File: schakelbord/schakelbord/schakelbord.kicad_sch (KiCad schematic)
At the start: 103 parts, among them J1 Rookmachine, J12 I/O nano, J15 Relais 7&8, J16 Alalog i/o, J17 Extra 1-4, J18 Extra 5-8, J19 Relais 5&6, J20 Relais 3&4, J21 Relais 1&2, J3 Power, J4 mosfets, K10 SANYOU_SRD_Form_C, K3 SANYOU_SRD_Form_C, K4 SANYOU_SRD_Form_C, K5 SANYOU_SRD_Form_C, K6 SANYOU_SRD_Form_C, K7 SANYOU_SRD_Form_C, K8 SANYOU_SRD_Form_C, K9 SANYOU_SRD_Form_C, Q1 BC547, Q10 BC337, Q11 BC337, Q12 BC337, Q13 BC337, Q14 BC337, Q4 Q_NMOS_GSD, Q5 BC337, Q6 BC337, Q7 Q_NMOS_GSD, Q8 Q_NMOS_GSD, Q9 BC337, U1 MCP23017x-x-SP

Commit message: pcb update
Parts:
- J1, J3: footprint PCM_SparkFun-Resistor:R_0603_1608Metric -> TerminalBlock_Phoenix:TerminalBlock_Phoenix_MKDS-1,5-2-5.08_1x02_P5.08mm_Horizontal
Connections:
- net at R47.1: now also D36.1 (K)
- net at D35.1 (K): now also R48.1
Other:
- moved on the sheet: D35, D36
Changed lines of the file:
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@@
 	)
 	(junction
-		(at 259.08 250.19)
+		(at 257.81 250.19)
 		(diameter 0)
 		(color 0 0 0 0)
@@
 	)
 	(junction
-		(at 252.73 250.19)
+		(at 251.46 250.19)
 		(diameter 0)
 		(color 0 0 0 0)
@@
 	(wire
 		(pts
-			(xy 259.08 250.19) (xy 264.16 250.19)
-		)
-		(stroke
-			(width 0)
-			(type default)
-		)
-	)
-	(wire
-		(pts
 			(xy 363.22 247.65) (xy 381 247.65)
 		)
@@
 	(wire
 		(pts
-			(xy 246.38 250.19) (xy 252.73 250.19)
+			(xy 246.38 250.19) (xy 264.16 250.19)
 		)
 		(stroke
@@
 	(wire
 		(pts
-			(xy 252.73 250.19) (xy 259.08 250.19)
-		)
-		(stroke
-			(width 0)
-			(type default)
-		)
-	)
-	(wire
-		(pts
 			(xy 87.63 255.27) (xy 91.44 255.27)
 		)
@@
 			)
 		)
-		(property "Footprint" "PCM_SparkFun-Resistor:R_0603_1608Metric"
+		(property "Footprint" "TerminalBlock_Phoenix:TerminalBlock_Phoenix_MKDS-1,5-2-5.08_1x02_P5.08mm_Horizontal"
 			(at 67.31 365.76 0)
 			(hide yes)
@@
 	(symbol
 		(lib_id "Device:LED")
-		(at 259.08 254 90)
+		(at 257.81 254 90)
 		(unit 1)
 		(body_style 1)
@@
 		(fields_autoplaced yes)
 		(property "Reference" "D35"
-			(at 256.54 256.8576 90)
+			(at 255.27 256.8576 90)
 			(show_name no)
 			(do_not_autoplace no)
@@
 		)
 		(property "Value" "LED"
-			(at 256.54 254.3176 90)
+			(at 255.27 254.3176 90)
 			(hide yes)
 			(show_name no)
@@
 		)
 		(property "Footprint" "LED_THT:LED_D5.0mm"
-			(at 259.08 254 0)
+			(at 257.81 254 0)
 			(hide yes)
 			(show_name no)
@@
 		)
 		(property "Datasheet" ""
-			(at 259.08 254 0)
+			(at 257.81 254 0)
 			(hide yes)
 			(show_name no)
@@
 		)
 		(property "Description" "Light emitting diode"
-			(at 259.08 254 0)
+			(at 257.81 254 0)
 			(hide yes)
 			(show_name no)
@@
 		)
 		(property "Sim.Pins" "1=K 2=A"
-			(at 259.08 254 0)
+			(at 257.81 254 0)
 			(hide yes)
 			(show_name no)
@@
 	(symbol
 		(lib_id "Device:LED")
-		(at 252.73 254 90)
+		(at 251.46 254 90)
 		(unit 1)
 		(body_style 1)
@@
 		(fields_autoplaced yes)
 		(property "Reference" "D36"
-			(at 250.19 256.8576 90)
+			(at 248.92 256.8576 90)
 			(show_name no)
 			(do_not_autoplace no)
@@
 		)
 		(property "Value" "LED"
-			(at 250.19 254.3176 90)
+			(at 248.92 254.3176 90)
 			(hide yes)
 			(show_name no)
@@
 		)
 		(property "Footprint" "LED_THT:LED_D5.0mm"
-			(at 252.73 254 0)
+			(at 251.46 254 0)
 			(hide yes)
 			(show_name no)
@@
 		)
 		(property "Datasheet" ""
-			(at 252.73 254 0)
+			(at 251.46 254 0)
 			(hide yes)
 			(show_name no)
@@
 		)
 		(property "Description" "Light emitting diode"
-			(at 252.73 254 0)
+			(at 251.46 254 0)
 			(hide yes)
 			(show_name no)
@@
 		)
 		(property "Sim.Pins" "1=K 2=A"
-			(at 252.73 254 0)
+			(at 251.46 254 0)
 			(hide yes)
 			(show_name no)
@@
 			)
 		)
-		(property "Footprint" "PCM_SparkFun-Resistor:R_0603_1608Metric"
+		(property "Footprint" "TerminalBlock_Phoenix:TerminalBlock_Phoenix_MKDS-1,5-2-5.08_1x02_P5.08mm_Horizontal"
 			(at 195.58 345.44 0)
 			(hide yes)

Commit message: pcb update
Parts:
- removed D15, D16: LED, LED_THT:LED_D5.0mm, symbol Device:LED
- removed Q4, Q7, Q8: Q_NMOS_GSD, PCM_SparkFun-Semiconductor-Standard:SC-89 SOT-490, symbol Transistor_FET:Q_NMOS_GSD
- removed R25, R28: 1K, Resistor_THT:R_Axial_DIN0204_L3.6mm_D1.6mm_P7.62mm_Horizontal, symbol Device:R
- added Q15, Q2, Q3: IRLZ44N, Package_TO_SOT_THT:TO-220-3_Vertical, symbol Transistor_FET:IRLZ44N
- added R61, R62: 470, Resistor_THT:R_Axial_DIN0204_L3.6mm_D1.6mm_P7.62mm_Horizontal, symbol Device:R
- Q1: value BC547 -> BC337
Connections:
- net +3.3V: now also R61.1, R62.1
- net GND: now also D17.1 (K), U1.15 (A0), U1.16 (A1), U1.17 (A2), Q15.3 (S), Q2.3 (S), Q3.3 (S)
- net at R23.2, R24.1: now also Q15.1 (G)
- net at R29.2, R30.1: now also Q2.1 (G)
- net at J4.1 (Pin_1): now also Q2.2 (D); no longer D17.1 (K)
- net at A1.23 (SDA/A4), U1.13 (SDA): now also R62.2
- net at A1.24 (SCL/A5), U1.12 (SCK): now also R61.2
- net at J4.2 (Pin_2): now also Q3.2 (D)
- net at R26.2, R27.1: now also Q3.1 (G)
- net at J4.3 (Pin_3): now also Q15.2 (D)
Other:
- moved on the sheet: J3

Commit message: pcb update
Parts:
- R61, R62: value 470 -> 4k7
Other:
- moved on the sheet: R8
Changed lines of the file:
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@@
 	)
 	(junction
+		(at 203.2 264.16)
+		(diameter 0)
+		(color 0 0 0 0)
+	)
+	(junction
 		(at 274.32 295.91)
 		(diameter 0)
@@
 	(wire
 		(pts
-			(xy 199.39 264.16) (xy 220.98 264.16)
+			(xy 199.39 264.16) (xy 203.2 264.16)
 		)
 		(stroke
@@
 	(wire
 		(pts
-			(xy 199.39 264.16) (xy 199.39 285.75)
-		)
-		(stroke
-			(width 0)
-			(type default)
-		)
-	)
-	(wire
-		(pts
 			(xy 389.89 287.02) (xy 398.78 287.02)
 		)
@@
 	(wire
 		(pts
+			(xy 203.2 274.32) (xy 203.2 300.99)
+		)
+		(stroke
+			(width 0)
+			(type default)
+		)
+	)
+	(wire
+		(pts
 			(xy 430.53 224.79) (xy 430.53 246.38)
 		)
@@
 	(wire
 		(pts
-			(xy 199.39 300.99) (xy 208.28 300.99)
-		)
-		(stroke
-			(width 0)
-			(type default)
-		)
-	)
-	(wire
-		(pts
 			(xy 233.68 303.53) (xy 316.23 303.53)
 		)
@@
 	(wire
 		(pts
+			(xy 203.2 264.16) (xy 203.2 266.7)
+		)
+		(stroke
+			(width 0)
+			(type default)
+		)
+	)
+	(wire
+		(pts
 			(xy 100.33 369.57) (xy 100.33 375.92)
 		)
@@
 	(wire
 		(pts
+			(xy 203.2 264.16) (xy 220.98 264.16)
+		)
+		(stroke
+			(width 0)
+			(type default)
+		)
+	)
+	(wire
+		(pts
 			(xy 233.68 285.75) (xy 251.46 285.75)
 		)
@@
 	(wire
 		(pts
+			(xy 203.2 300.99) (xy 208.28 300.99)
+		)
+		(stroke
+			(width 0)
+			(type default)
+		)
+	)
+	(wire
+		(pts
 			(xy 316.23 303.53) (xy 316.23 152.4)
 		)
@@
 	(wire
 		(pts
-			(xy 199.39 293.37) (xy 199.39 300.99)
-		)
-		(stroke
-			(width 0)
-			(type default)
-		)
-	)
-	(wire
-		(pts
 			(xy 335.28 316.23) (xy 335.28 308.61)
 		)
@@
 		(in_pos_files yes)
 		(dnp no)
-		(fields_autoplaced yes)
 		(property "Reference" "R61"
-			(at 181.61 271.7801 0)
-			(hide yes)
+			(at 189.484 268.224 0)
 			(show_name no)
 			(do_not_autoplace no)
@@
 			)
 		)
-		(property "Value" "470"
+		(property "Value" "4k7"
 			(at 186.69 270.5099 0)
 			(show_name no)
@@
 	(symbol
 		(lib_id "Device:R")
-		(at 199.39 289.56 0)
+		(at 203.2 270.51 0)
 		(unit 1)
 		(body_style 1)
@@
 		(fields_autoplaced yes)
 		(property "Reference" "R8"
-			(at 201.93 288.2899 0)
+			(at 205.74 269.2399 0)
 			(show_name no)
 			(do_not_autoplace no)
@@
 		)
 		(property "Value" "10k"
-			(at 201.93 290.8299 0)
+			(at 205.74 271.7799 0)
 			(show_name no)
 			(do_not_autoplace no)
@@
 		)
 		(property "Footprint" "Resistor_THT:R_Axial_DIN0204_L3.6mm_D1.6mm_P7.62mm_Horizontal"
-			(at 197.612 289.56 90)
+			(at 201.422 270.51 90)
 			(hide yes)
 			(show_name no)
@@
 		)
 		(property "Datasheet" ""
-			(at 199.39 289.56 0)
+			(at 203.2 270.51 0)
 			(hide yes)
 			(show_name no)
@@
 		)
 		(property "Description" "Resistor"
-			(at 199.39 289.56 0)
+			(at 203.2 270.51 0)
 			(hide yes)
 			(show_name no)
@@
 		(in_pos_files yes)
 		(dnp no)
-		(fields_autoplaced yes)
 		(property "Reference" "R62"
-			(at 191.77 271.7801 0)
-			(hide yes)
+			(at 199.39 268.478 0)
 			(show_name no)
 			(do_not_autoplace no)
@@
 			)
 		)
-		(property "Value" "470"
+		(property "Value" "4k7"
 			(at 196.85 270.5099 0)
 			(show_name no)

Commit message: pcb update
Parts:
- removed D10, D11, D12: LED, LED_THT:LED_D5.0mm, symbol Device:LED
- removed R14, R15, R16: 1K, Resistor_THT:R_Axial_DIN0204_L3.6mm_D1.6mm_P7.62mm_Horizontal, symbol Device:R

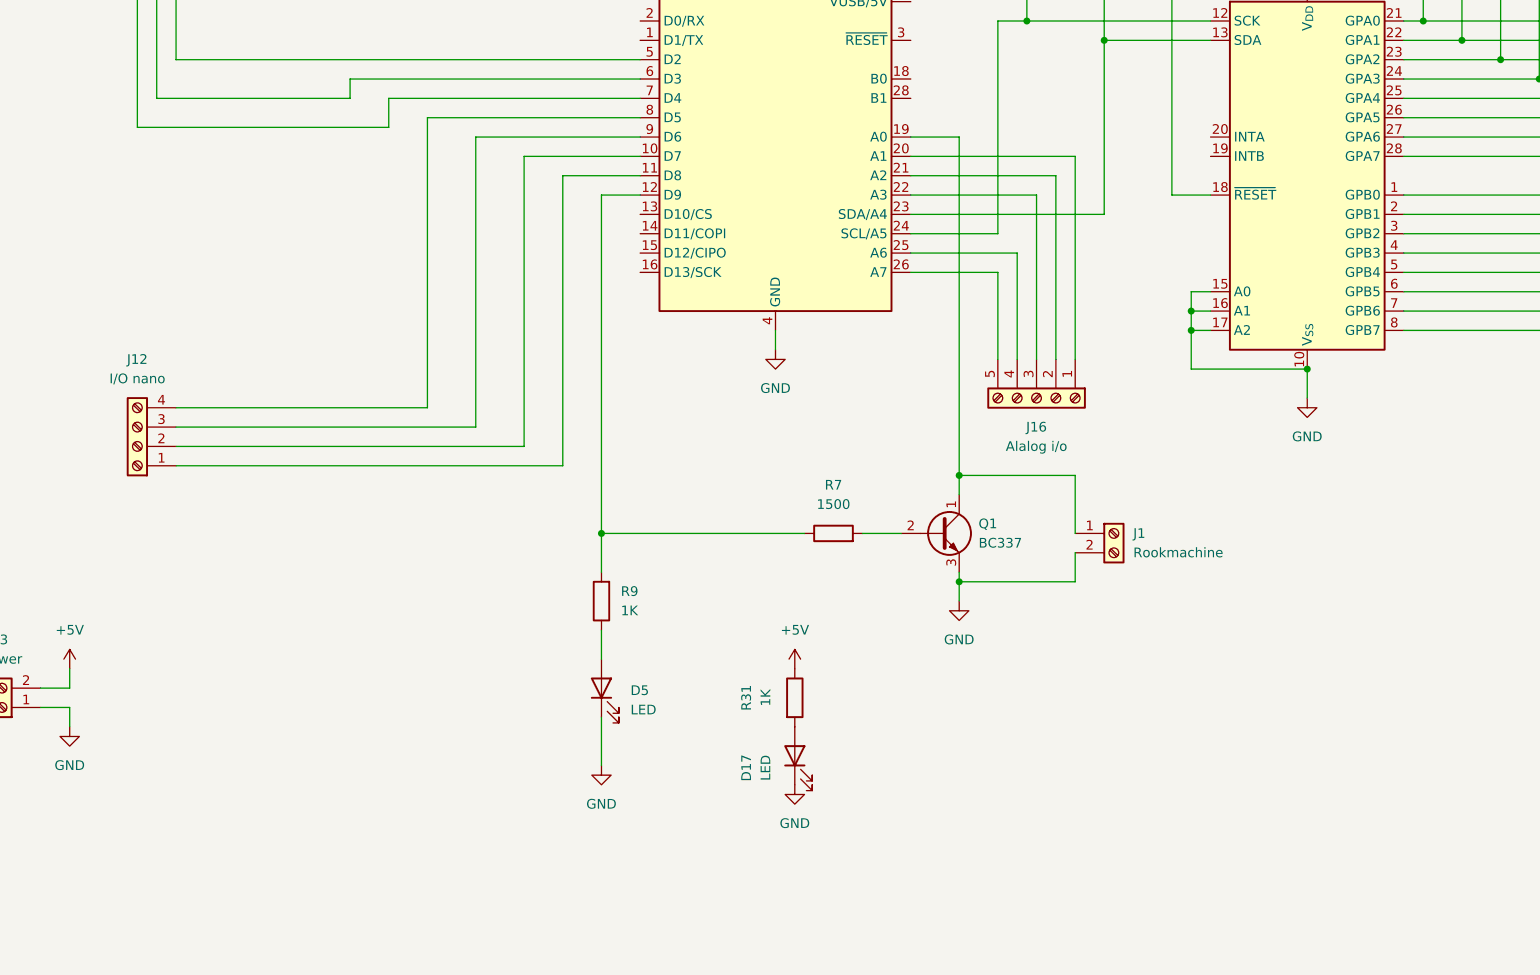
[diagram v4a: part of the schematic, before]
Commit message: Add option to detect if smoke machine is turned on
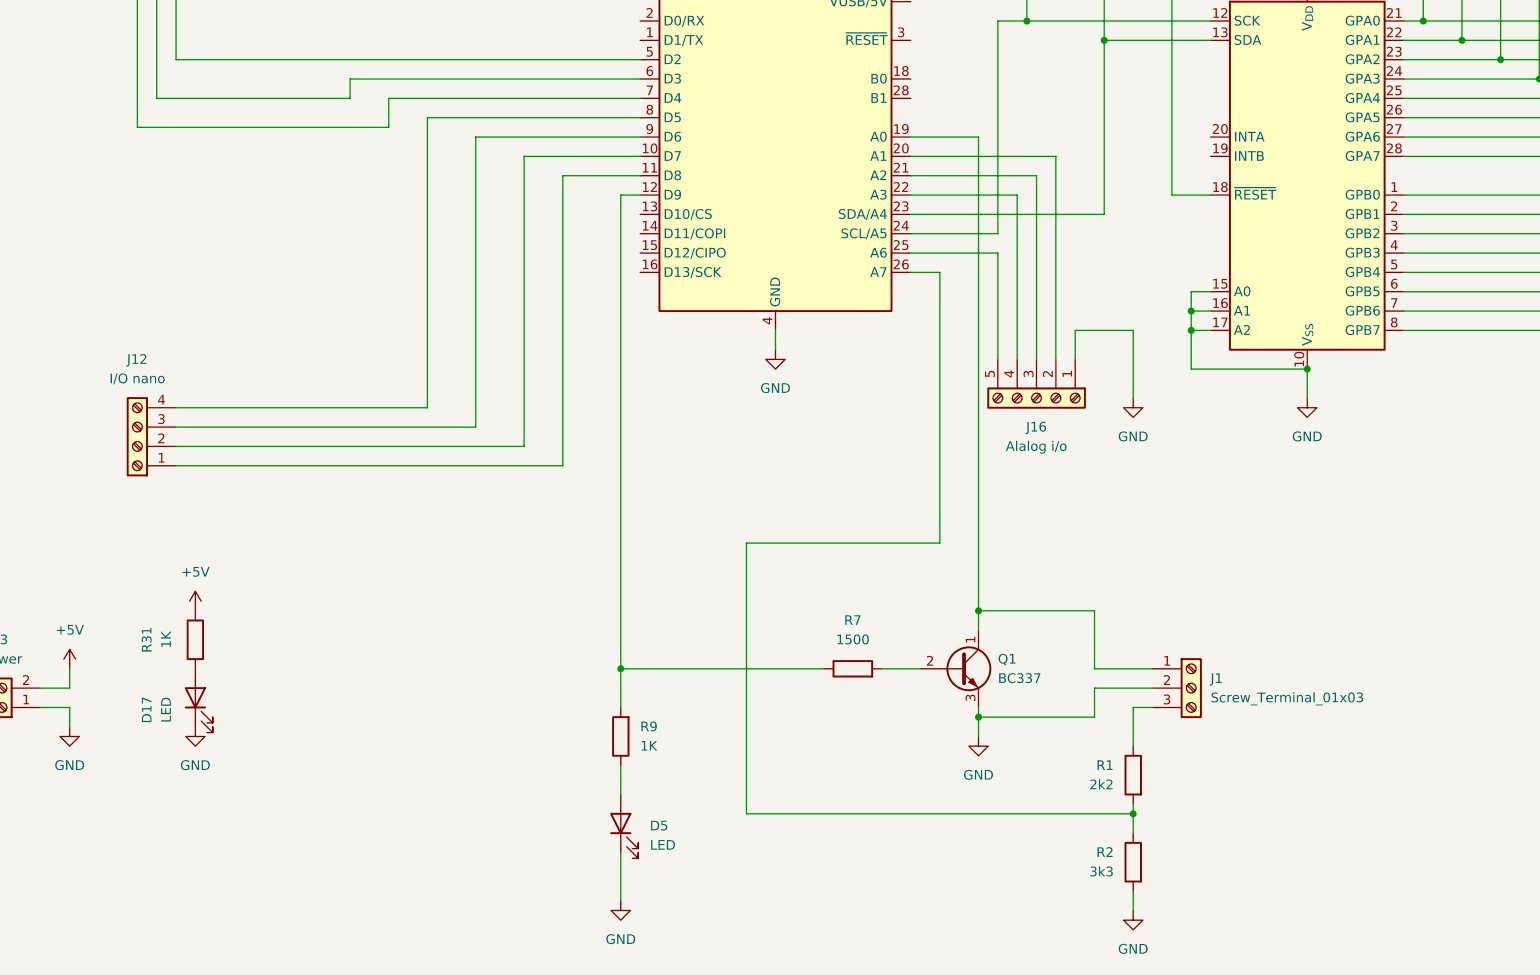
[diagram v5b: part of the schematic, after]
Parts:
- removed J1: Rookmachine, TerminalBlock_Phoenix:TerminalBlock_Phoenix_MKDS-1,5-2-5.08_1x02_P5.08mm_Horizontal, symbol Connector:Screw_Terminal_01x02
- added J1: Screw_Terminal_01x03, symbol Connector:Screw_Terminal_01x03
- added R1: 2k2, symbol Device:R
- added R2: 3k3, symbol Device:R
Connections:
- net GND: now also J16.1 (Pin_1), J1.2 (Pin_2), R2.2
- net at A1.19 (A0), Q1.1 (C): now also J1.1 (Pin_1)
- net at A1.20 (A1): now also J16.2 (Pin_2); no longer J16.1 (Pin_1)
- net at A1.21 (A2): now also J16.3 (Pin_3); no longer J16.2 (Pin_2)
- net at A1.22 (A3): now also J16.4 (Pin_4); no longer J16.3 (Pin_3)
- net at A1.25 (A6): now also J16.5 (Pin_5); no longer J16.4 (Pin_4)
- net at A1.26 (A7): now also R1.2, R2.1; no longer J16.5 (Pin_5)
- new net: J1.3 (Pin_3), R1.1
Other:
- moved on the sheet: D17, D5, Q1, R31, R7, R9

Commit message: pcb update
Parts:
- added D49, D50, D51, D52, D53, D54, D55: LED, LED_THT:LED_D5.0mm, symbol Device:LED
- added R63, R64, R65, R66, R67, R68, R69: 1K, Resistor_THT:R_Axial_DIN0204_L3.6mm_D1.6mm_P7.62mm_Horizontal, symbol Device:R
- J1: footprint (none) -> TerminalBlock_Phoenix:TerminalBlock_Phoenix_MKDS-1,5-3-5.08_1x03_P5.08mm_Horizontal
- J4: footprint (none) -> TerminalBlock_Phoenix:TerminalBlock_Phoenix_MKDS-1,5-3_1x03_P5.00mm_Horizontal
- R1, R2: footprint (none) -> Resistor_THT:R_Axial_DIN0204_L3.6mm_D1.6mm_P7.62mm_Horizontal
- R9: footprint Resistor_THT:R_Axial_DIN0204_L3.6mm_D1.6mm_P7.62mm_Horizontal -> Resistor_THT:R_Axial_DIN0207_L6.3mm_D2.5mm_P10.16mm_Horizontal
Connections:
- net +3.3V: no longer D32.2 (A), D33.2 (A), D34.2 (A), D35.2 (A), D36.2 (A), D37.2 (A), D38.2 (A), D39.2 (A)
- net +5V: now also D32.2 (A), D33.2 (A), D34.2 (A), D35.2 (A), D36.2 (A), D37.2 (A), D38.2 (A), D39.2 (A), D49.2 (A), D50.2 (A), D51.2 (A), D52.2 (A), D53.2 (A), D54.2 (A), D55.2 (A)
- net GND: now also J16.5 (Pin_5); no longer J16.1 (Pin_1)
- net at A1.10 (D7), J12.2 (Pin_2): now also R64.2
- net at A1.11 (D8), J12.1 (Pin_1): now also R63.2
- net at A1.20 (A1): now also J16.1 (Pin_1); no longer J16.2 (Pin_2)
- net at A1.21 (A2): now also J16.2 (Pin_2); no longer J16.3 (Pin_3)
- net at A1.22 (A3): now also J16.3 (Pin_3); no longer J16.4 (Pin_4)
- net at A1.25 (A6): now also J16.4 (Pin_4); no longer J16.5 (Pin_5)
- net at A1.5 (D2), R23.1: now also R69.2
- net at A1.6 (D3), R26.1: now also R68.2
- net at A1.7 (D4), R29.1: now also R67.2
- net at A1.8 (D5), J12.4 (Pin_4): now also R66.2
- net at A1.9 (D6), J12.3 (Pin_3): now also R65.2
- new net: D50.1 (K), R64.1
- new net: D55.1 (K), R69.1
- new net: D52.1 (K), R66.1
- new net: D54.1 (K), R68.1
- new net: D51.1 (K), R65.1
- new net: D53.1 (K), R67.1
- new net: D49.1 (K), R63.1
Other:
- moved on the sheet: D17, J16, J3, J4, Q15, Q2, Q3, R23, R24, R26, R27, R29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

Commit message: pcb update
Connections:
- net +3.3V: now also D49.2 (A), D50.2 (A), D51.2 (A), D52.2 (A)
- net +5V: no longer D49.2 (A), D50.2 (A), D51.2 (A), D52.2 (A), D53.2 (A), D54.2 (A), D55.2 (A)
- net GND: now also D53.1 (K), D54.1 (K), D55.1 (K)
- net at R69.1: now also A1.7 (D4), R29.1; no longer D55.1 (K)
- net at A1.5 (D2), R23.1: now also R67.1; no longer R69.2
- net at A1.6 (D3), R26.1: now also R68.1; no longer R68.2
- new net: D55.2 (A), R69.2
- new net: D54.2 (A), R68.2
- new net: D53.2 (A), R67.2
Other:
- moved on the sheet: D53, D54, D55

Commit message: pcb update
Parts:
- added C1: 0.1uF, PCM_SparkFun-Capacitor:C_0402_1005Metric, symbol PCM_SparkFun-Capacitor:0.1uF_0402_16V_10%
- added C2: 470uF, PCM_SparkFun-Capacitor:Electrolytic_10.3x10.3mm, symbol PCM_SparkFun-Capacitor:470uF_10x10_25V_20%
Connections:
- net +3.3V: now also D32.2 (A), D33.2 (A), D34.2 (A), D35.2 (A), D36.2 (A), D37.2 (A), D38.2 (A), D39.2 (A), C1.2
- net +5V: now also C2.1; no longer D32.2 (A), D33.2 (A), D34.2 (A), D35.2 (A), D36.2 (A), D37.2 (A), D38.2 (A), D39.2 (A)
- net GND: now also C1.1, C2.2
